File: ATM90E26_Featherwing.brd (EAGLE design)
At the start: 49.9 x 39.4 mm, 60 parts, among them J1 ST-PJ-312, J2 4P-SMD-2.0-90D, J3 4P-SMD-2.0-90D, J4 12V AC, Q1 8.192MHz, U1 ATM90E26, U2 CJT1117-5.0-SOT223

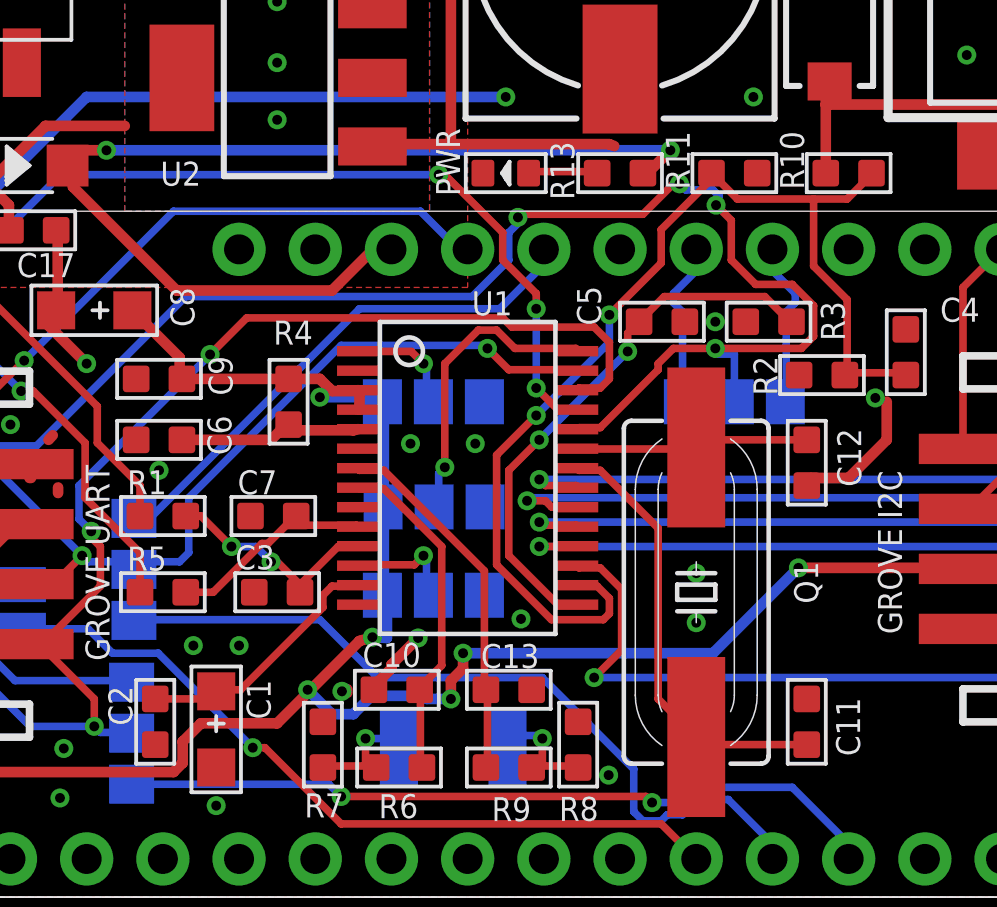
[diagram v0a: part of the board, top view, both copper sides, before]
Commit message: Routing feasibility analysed, relay/resize jumpers
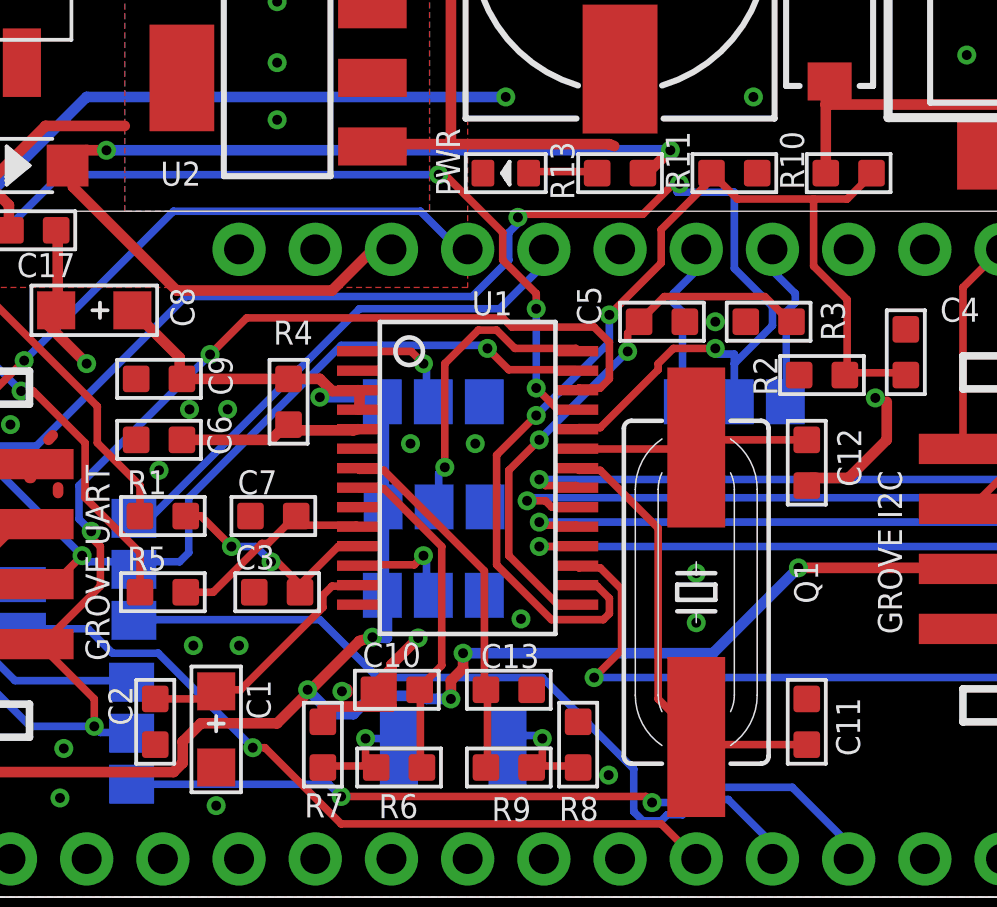
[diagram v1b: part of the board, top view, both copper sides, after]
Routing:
- net GND: track 62.2 -> 66.3 mm, vias 30 -> 32
- net CS: track 57.3 -> 54.6 mm, vias 6 -> 5

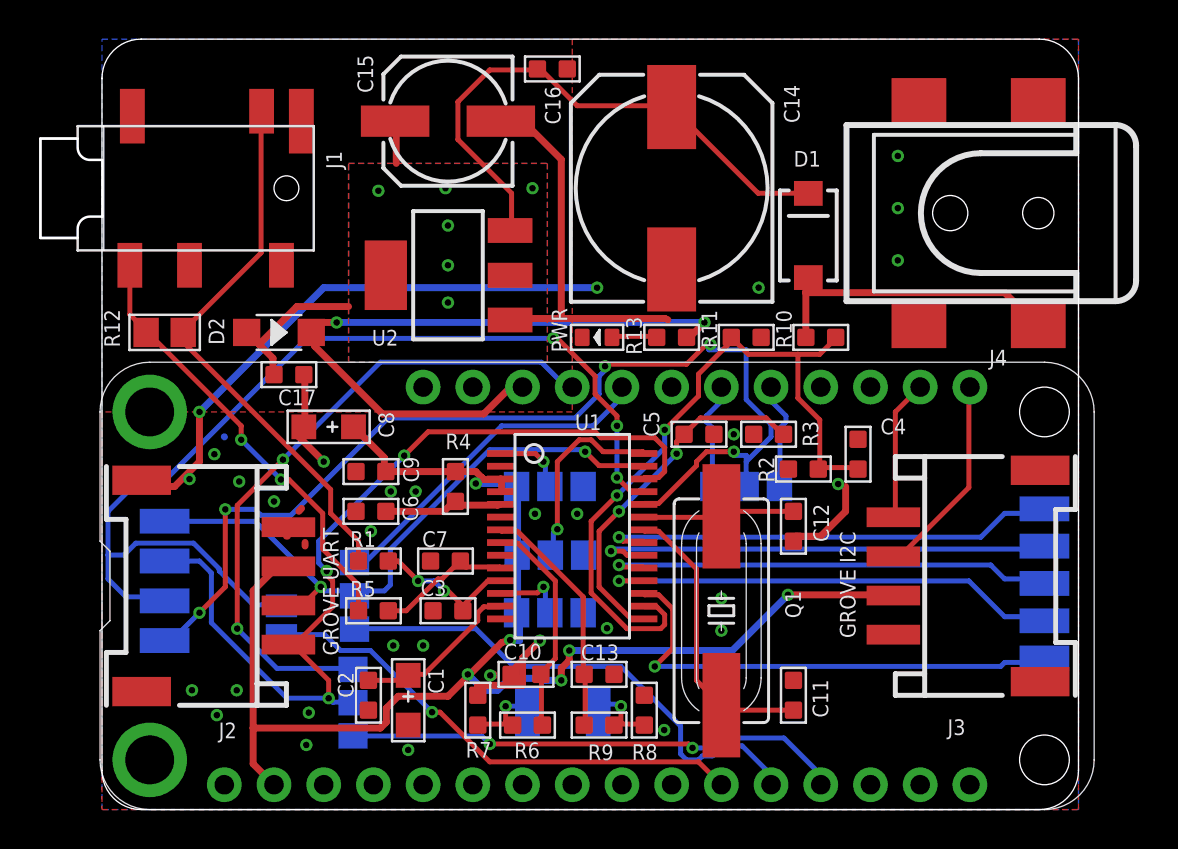
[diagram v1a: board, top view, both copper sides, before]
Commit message: Used smaller solder jumpers and finished route, bumped version
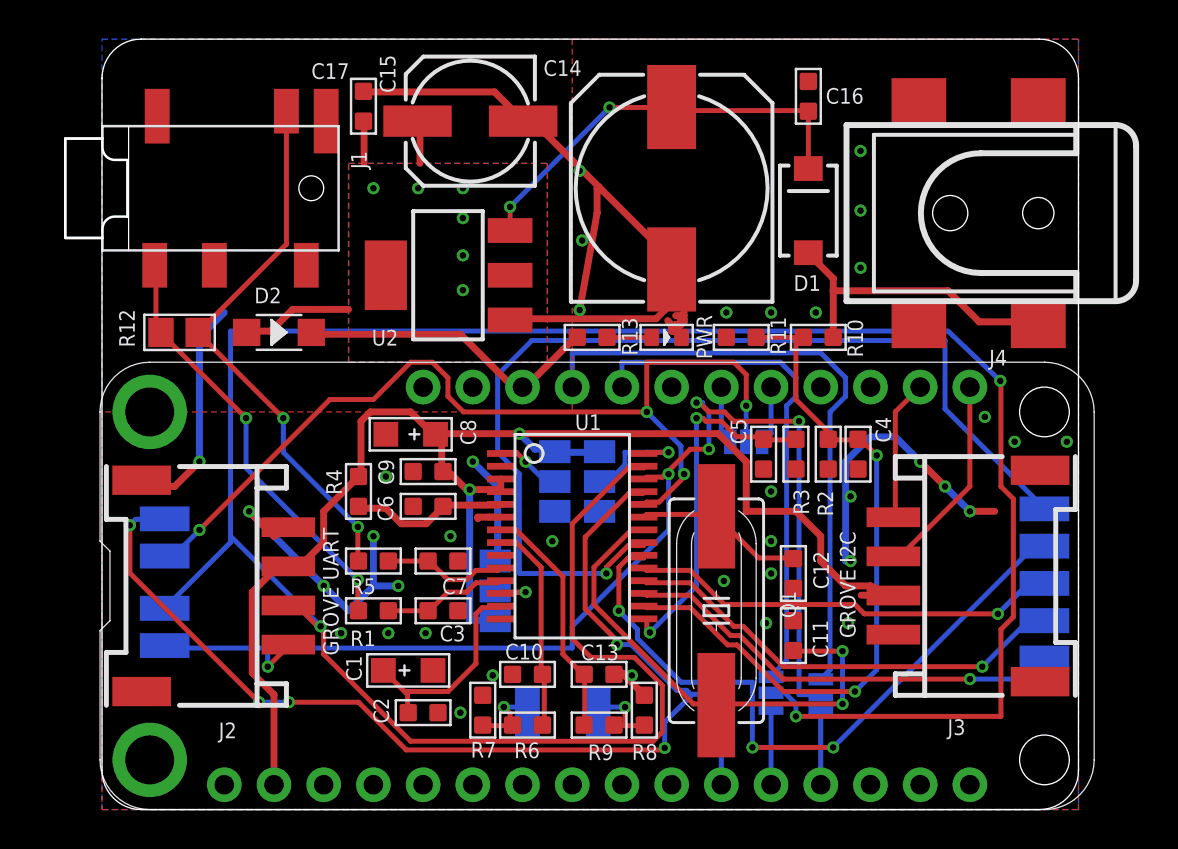
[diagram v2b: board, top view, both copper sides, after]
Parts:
- removed MIMUX, MOMUX: 0R-JUMPA, jump-0r-smd:A0R-JMP
- removed SCK: SCK, jumper:SJ
- added RXMUX, TXMUX: JUMPER-PAD-3-NOYES_SILK, SparkFun-Passives:PAD-JUMPER-3-NO_YES_SILK
- added SCKMUX: JUMPER-PAD-2-NOYES_SILK, SparkFun-Passives:PAD-JUMPER-2-NO_YES_SILK
- CSMUX: value 0R-JUMPA -> JUMPER-PAD-3-NOYES_SILK; device jump-0r-smd:A0R-JMP -> SparkFun-Passives:PAD-JUMPER-3-NO_YES_SILK
- MMD0, MMD1, USEL: value 0R-JUMPA -> JUMPER-PAD-3-NOFULL_BOX_SILK; device jump-0r-smd:A0R-JMP -> SparkFun-Passives:PAD-JUMPER-3-NO_YES_SILK_FULL_BOX
- moved LOGO1 42.1 mm to (5.59, 31.9), turned to 270 degrees
- moved C17 14.2 mm to (13.5, 35.9), turned to 270 degrees
- moved C16 13.2 mm to (36.2, 36.4), turned to 270 degrees
- moved R4 4.96 mm to (13.2, 16.3)
- moved MMD0 4.52 mm to (25.5, 16.8), turned to 90 degrees
- moved SI/RX 4.44 mm to (3.30, 10.3)
- moved CS 4.32 mm to (3.30, 13.0)
- moved SO/TX 4.32 mm to (3.30, 8.38)
- moved C8 4.21 mm to (15.9, 19.2)
- moved SCLK 4.19 mm to (3.30, 14.9)
- moved R13 4.06 mm to (25.1, 24.1), turned to 90 degrees
- moved PWR 3.56 mm to (29.0, 24.1), turned to 0 degrees
- moved C5 3.45 mm to (33.9, 18.2), turned to 90 degrees
- moved C11 3.05 mm to (35.4, 8.89)
- moved USEL 3.01 mm to (20.2, 11.2)
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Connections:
- net +3V3: now also MMD0.3, MMD1.1, USEL.3; no longer MMD0.1, MMD1.3, USEL.1
- net ATM_RX: now also RXMUX.3; no longer MOMUX.1
- net ATM_TX: now also TXMUX.3; no longer MIMUX.1
- net CS_10: now also CSMUX.3; no longer CSMUX.1
- net CS_9: now also CSMUX.1; no longer CSMUX.3
- net GND: now also MMD0.1, MMD1.3, USEL.1; no longer MMD0.3, MMD1.1, USEL.3
- net I1N_IN: now also J1.L, R12.2; no longer J1.COM1, R12.1
- net I1P_IN: now also J1.COM1, R12.1; no longer J1.L, R12.2
- net MISO: now also TXMUX.1; no longer MIMUX.3
- net MOSI: now also RXMUX.1; no longer MOMUX.3
- net SCK: now also SCKMUX.1; no longer SCK.2
- net SCLK: now also SCKMUX.2; no longer SCK.1
- net SI/RX: now also RXMUX.2; no longer MOMUX.2
- net SO/TX: now also TXMUX.2; no longer MIMUX.2
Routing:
- net SI/RX: track 32.6 -> 134.6 mm, vias 2 -> 3
- net N$20: track 23.7 -> 52.2 mm
- net GND: track 66.3 -> 93.9 mm, vias 32 -> 38
- net MOSI: track 26.3 -> 3.89 mm
- net SCK: track 25.7 -> 3.74 mm, vias 1 -> 0
- net MISO: track 25.7 -> 3.76 mm, vias 2 -> 0
- net USB: track 35.0 -> 15.9 mm, vias 2 -> 0
- net SO/TX: track 47.3 -> 62.1 mm, vias 3 -> 5
- net N$21: track 24.0 -> 35.0 mm, vias 1 -> 3
- net CLKIN: track 14.8 -> 25.3 mm, vias 0 -> 2
- net ATM_RX: track 17.7 -> 26.3 mm
- net N$4: track 29.0 -> 21.6 mm, vias 0 -> 2
- net I1P_IN: track 28.4 -> 22.0 mm, vias 0 -> 2
- net CS: track 54.6 -> 48.4 mm, vias 5 -> 4
- net I1N_IN: track 22.8 -> 28.3 mm
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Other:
- board text added: "SCK,MOSI,MISO used in SPI mode. CS on pin 9 or 10. UART uses pins 12 - RX, 13 - TX"

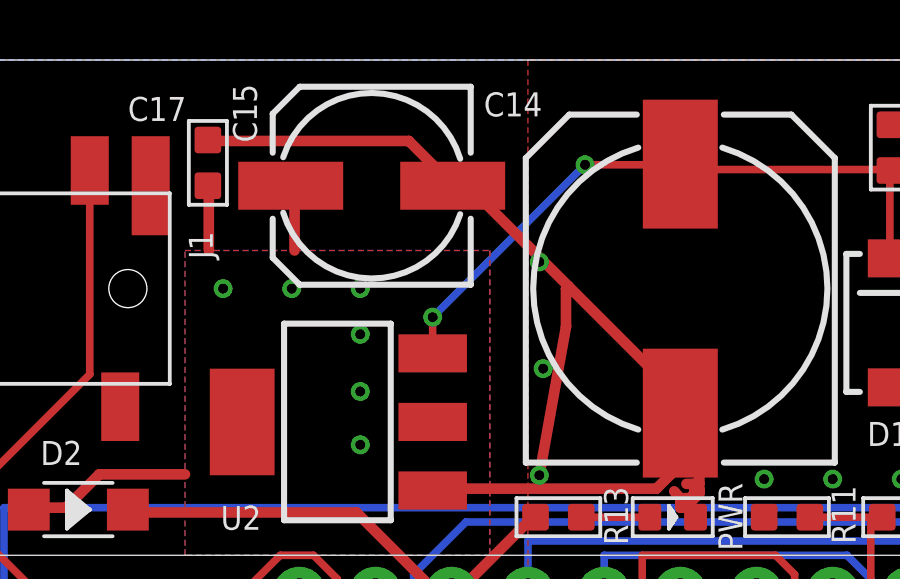
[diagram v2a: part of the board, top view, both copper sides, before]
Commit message: Create continous thermal plane for LDO
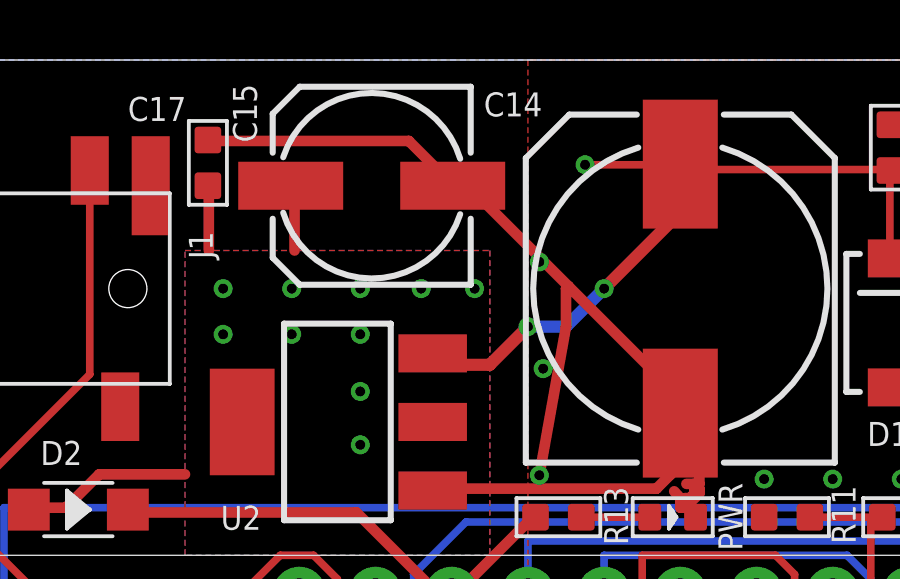
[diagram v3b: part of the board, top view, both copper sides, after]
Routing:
- net N$4: track 21.6 -> 25.3 mm, vias 2 -> 3
- net V_OUT: vias 6 -> 10
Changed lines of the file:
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@@
 <?xml version="1.0" encoding="utf-8"?>
 <!DOCTYPE eagle SYSTEM "eagle.dtd">
-<eagle version="7.4.0">
+<eagle version="7.6.0">
 <drawing>
 <settings>
@@
 <contactref element="C16" pad="2"/>
 <wire x1="36.195" y1="32.757" x2="36.195" y2="35.687" width="0.254" layer="1"/>
-<wire x1="20.955" y1="30.7975" x2="20.955" y2="29.591" width="0.254" layer="1"/>
-<wire x1="26.035" y1="35.8775" x2="20.955" y2="30.7975" width="0.254" layer="16"/>
 <wire x1="29.21" y1="35.8775" x2="26.035" y2="35.8775" width="0.254" layer="1"/>
 <wire x1="29.36875" y1="35.71875" x2="36.195" y2="35.71875" width="0.254" layer="1"/>
@@
 <wire x1="36.195" y1="35.71875" x2="36.195" y2="35.687" width="0.254" layer="1"/>
 <wire x1="29.21" y1="35.8775" x2="29.21" y2="35.9" width="0.254" layer="1"/>
-<via x="20.955" y="30.7975" extent="1-16" drill="0.3302"/>
 <via x="26.035" y="35.8775" extent="1-16" drill="0.3302"/>
+<wire x1="26.67" y1="31.75" x2="25.4" y2="30.48" width="0.4064" layer="16"/>
+<wire x1="29.21" y1="34.29" x2="26.67" y2="31.75" width="0.4064" layer="1"/>
+<wire x1="29.21" y1="35.9" x2="29.21" y2="34.29" width="0.4064" layer="1"/>
+<wire x1="24.13" y1="30.48" x2="25.4" y2="30.48" width="0.4064" layer="16"/>
+<wire x1="22.86" y1="29.21" x2="24.13" y2="30.48" width="0.4064" layer="1"/>
+<wire x1="21.59" y1="29.21" x2="22.86" y2="29.21" width="0.4064" layer="1"/>
+<wire x1="21.59" y1="29.21" x2="20.955" y2="29.591" width="0.4064" layer="1"/>
+<via x="26.67" y="31.75" extent="1-16" drill="0.3302"/>
+<via x="24.13" y="30.48" extent="1-16" drill="0.3302"/>
 </signal>
 <signal name="V_OUT" class="1">
@@
 <via x="18.542" y="28.321" extent="1-16" drill="0.3302"/>
 <via x="18.542" y="26.543" extent="1-16" drill="0.3302"/>
+<via x="22.352" y="31.75" extent="1-16" drill="0.3302"/>
+<via x="20.574" y="31.75" extent="1-16" drill="0.3302"/>
+<via x="13.97" y="30.226" extent="1-16" drill="0.3302"/>
+<via x="16.256" y="30.226" extent="1-16" drill="0.3302"/>
 </signal>
 <signal name="USB" class="1">

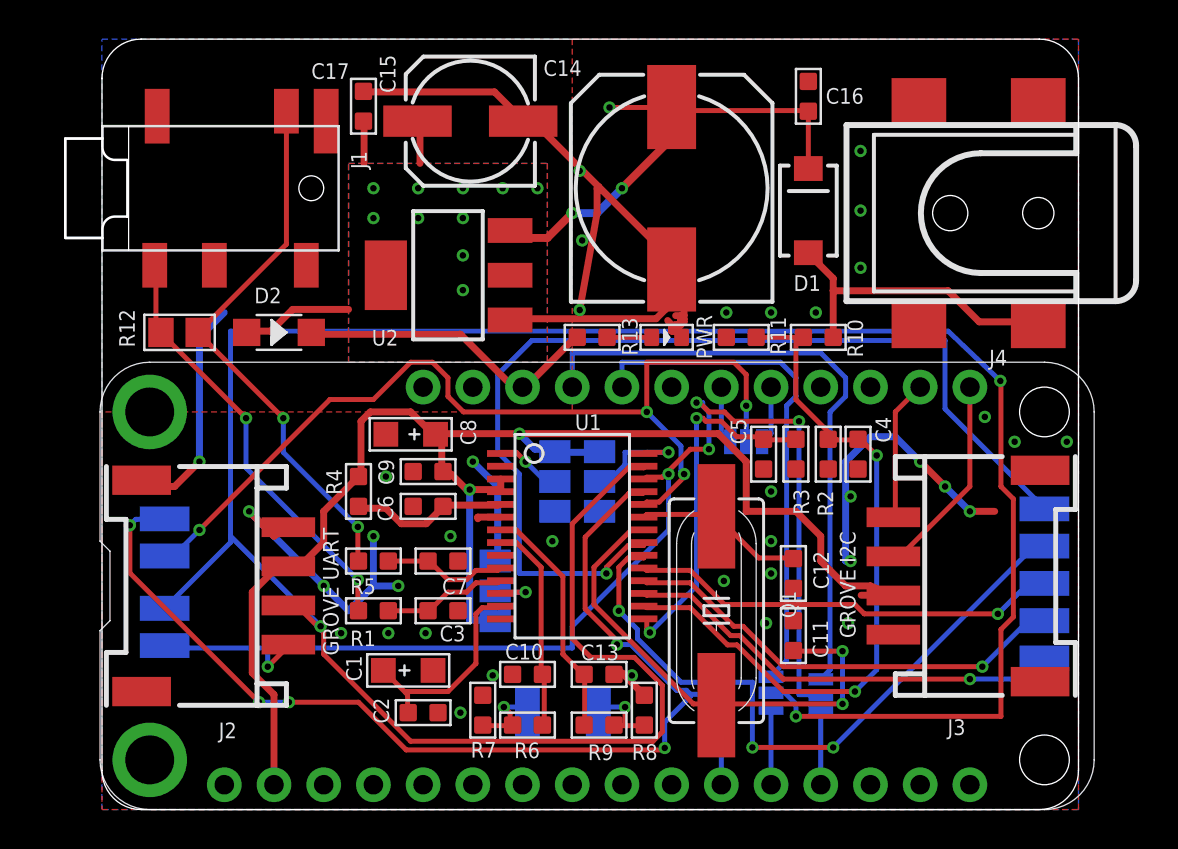
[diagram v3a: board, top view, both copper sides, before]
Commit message: Rerouted to new UART pins
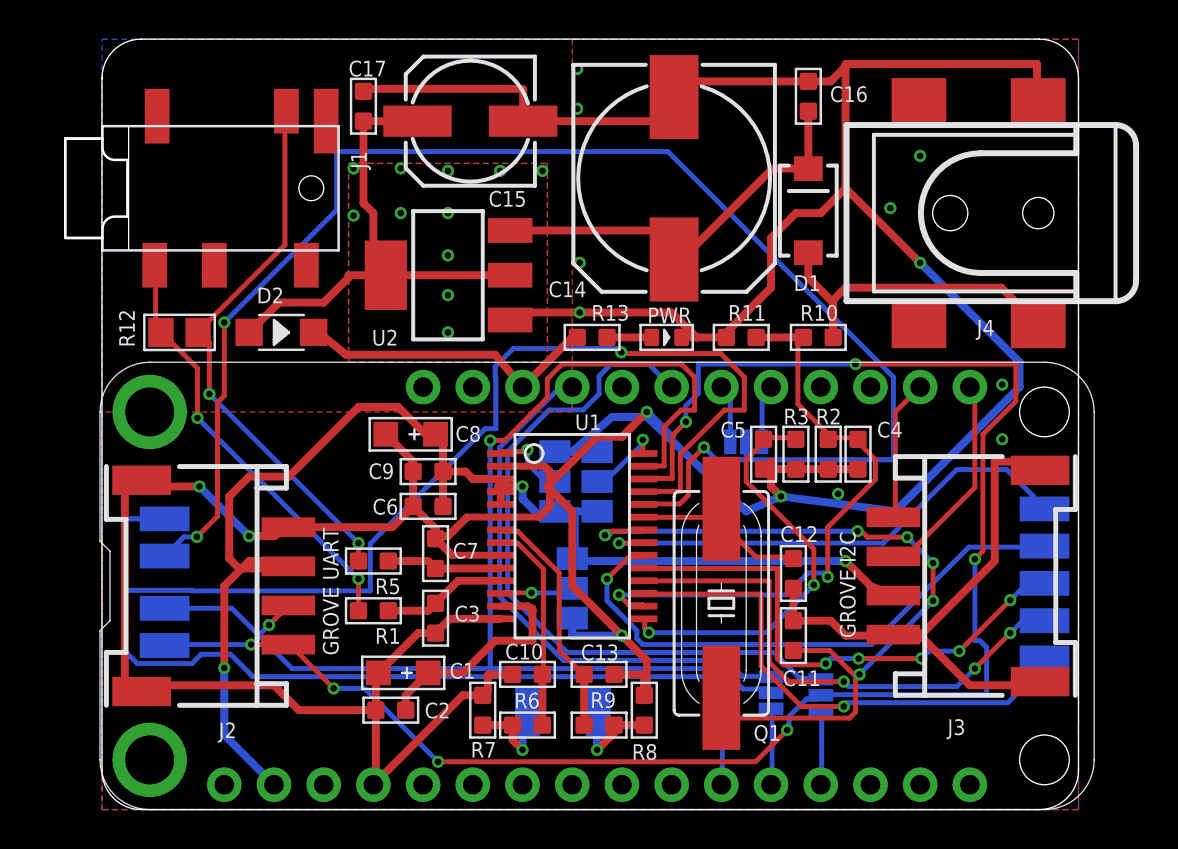
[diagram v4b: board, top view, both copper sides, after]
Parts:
- removed R4: 0R, Seeed-Resistor-2016:R0603
- moved USEL 3.94 mm to (24.1, 11.3), turned to 90 degrees
- moved C2 1.66 mm to (14.9, 5.08), turned to 0 degrees
- moved C3 0.54 mm to (17.1, 9.78), turned to 90 degrees
- moved C7 0.54 mm to (17.1, 13.1), turned to 90 degrees
- moved C14 0.52 mm to (29.3, 32.3), turned to 270 degrees
- moved Q1 0.46 mm to (31.8, 10.5)
- moved C1 0.28 mm to (15.5, 6.99), turned to 180 degrees
- moved MMD0 0.13 mm to (25.4, 16.8), turned to 270 degrees
- moved D2 0.13 mm to (9.27, 24.4)
- turned MMD1 to 90 degrees
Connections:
- removed net N$6: C6.2, R4.1, U1.5
- net +3V3: now also C6.2, U1.5; no longer R4.2
- net ATM_RX: now also MS1.25; no longer MS1.24
- net ATM_TX: now also MS1.23; no longer MS1.25
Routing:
- net GND: track 93.9 -> 261.6 mm, vias 38 -> 15
- net SI/RX: track 134.6 -> 66.1 mm, vias 3 -> 2
- net SCLK: track 55.3 -> 90.9 mm, vias 5 -> 1
- net CS: track 48.4 -> 78.3 mm, vias 4 -> 3
- net N$20: track 52.2 -> 25.5 mm
- net SO/TX: track 62.1 -> 88.6 mm, vias 5 -> 7
- net V_OUT: track 10.1 -> 25.5 mm, vias 10 -> 11
- net CLKIN: track 25.3 -> 40.7 mm, vias 2 -> 6
- net N$6: track 8.03 -> 0.00 mm
- net +3V3: track 75.7 -> 68.5 mm, vias 2 -> 3
- net N$21: track 35.0 -> 29.1 mm, vias 3 -> 1
- net VP: track 37.1 -> 31.2 mm
- net N$12: track 22.2 -> 27.0 mm, vias 1 -> 5
- net ATM_TX: track 32.2 -> 36.3 mm
- net N$4: track 25.3 -> 21.2 mm, vias 3 -> 0
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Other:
- board text added: "SCK,MOSI,MISO used in SPI mode. CS on pin 9 or 10. UART uses pins 11-RX, 13-TX (13-RX,14-TX Huzzah)"
- board text removed: "SCK,MOSI,MISO used in SPI mode. CS on pin 9 or 10. UART uses pins 12 - RX, 13 - TX"
